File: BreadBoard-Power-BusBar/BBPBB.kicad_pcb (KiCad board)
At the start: 4 copper layers, 53.6 x 5.2 mm, 2 parts, among them J1 Conn_02x02_Odd_Even, J2 Conn_02x02_Odd_Even

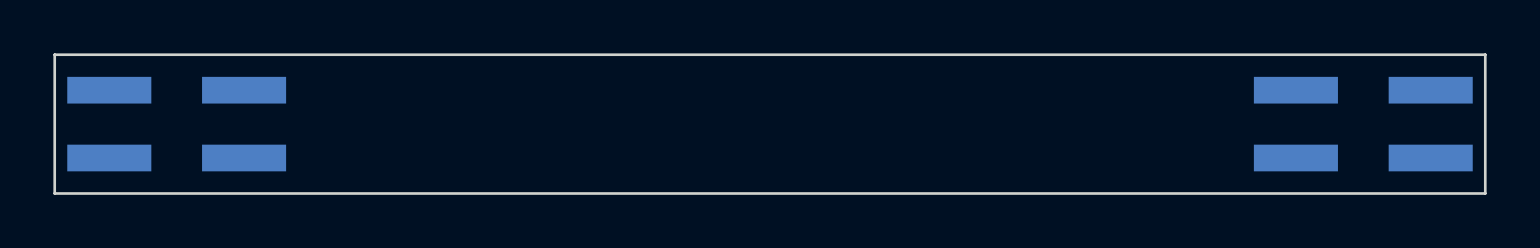
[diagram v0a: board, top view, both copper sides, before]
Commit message: Routed all the power nets through the inner layers.
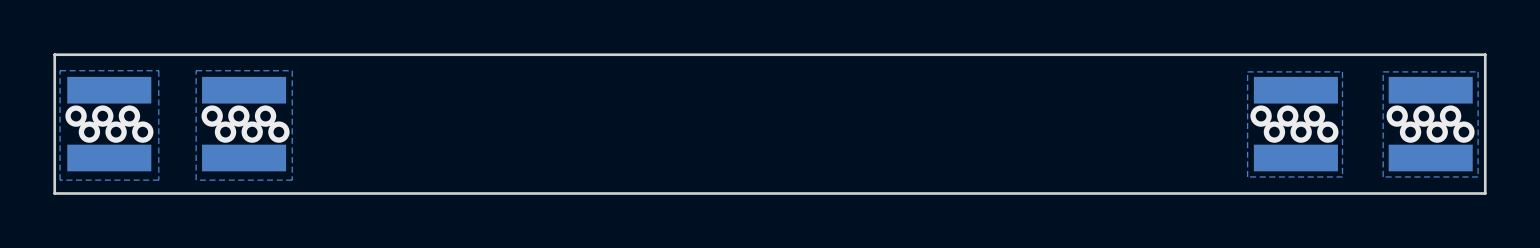
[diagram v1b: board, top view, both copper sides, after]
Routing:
- net /Power-2: vias 0 -> 12
- net /Power-1: vias 0 -> 12
- added copper zone on B.Cu, net /Power-1
- added copper zone on In1.Cu, net /Power-1
- added copper zone on B.Cu, net /Power-2
- added copper zone on In2.Cu, net /Power-2
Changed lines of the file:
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@@
     (thickness 1.6)
     (drawings 9)
-    (tracks 0)
+    (tracks 24)
     (zones 0)
     (modules 2)
@@
   )
   (layers
-    (0 Front signal)
+    (0 F.Cu signal)
     (1 In1.Cu signal)
     (2 In2.Cu signal)
-    (31 Back signal)
+    (31 B.Cu signal)
     (34 B.Paste user)
     (35 F.Paste user)
@@
     (add_net /Power-2)
   )
-  (module Connector_PinHeader_2.54mm:PinHeader_2x02_P2.54mm_Vertical_SMD (layer Back)
+  (module Connector_PinHeader_2.54mm:PinHeader_2x02_P2.54mm_Vertical_SMD (layer B.Cu)
     (at 127.77 100)
     (descr "surface-mounted straight pin header, 2x02, 2.54mm pitch, double rows")
@@
       (effects (font (size 1 1) (thickness 0.15)) (justify mirror))
     )
-    (pad 1 smd rect (at -2.525 1.27) (size 3.15 1) (layers Back B.Paste B.Mask)
+    (pad 1 smd rect (at -2.525 1.27) (size 3.15 1) (layers B.Cu B.Paste B.Mask)
       (net 1 /Power-2))
-    (pad 2 smd rect (at 2.525 1.27) (size 3.15 1) (layers Back B.Paste B.Mask)
+    (pad 2 smd rect (at 2.525 1.27) (size 3.15 1) (layers B.Cu B.Paste B.Mask)
       (net 2 /Power-1))
-    (pad 3 smd rect (at -2.525 -1.27) (size 3.15 1) (layers Back B.Paste B.Mask)
+    (pad 3 smd rect (at -2.525 -1.27) (size 3.15 1) (layers B.Cu B.Paste B.Mask)
       (net 1 /Power-2))
-    (pad 4 smd rect (at 2.525 -1.27) (size 3.15 1) (layers Back B.Paste B.Mask)
+    (pad 4 smd rect (at 2.525 -1.27) (size 3.15 1) (layers B.Cu B.Paste B.Mask)
       (net 2 /Power-1))
     (model ${KISYS3DMOD}/Connector_PinHeader_2.54mm.3dshapes/PinHeader_2x02_P2.54mm_Vertical_SMD.wrl
@@
     )
   )
-  (module Connector_PinHeader_2.54mm:PinHeader_2x02_P2.54mm_Vertical_SMD (layer Back)
+  (module Connector_PinHeader_2.54mm:PinHeader_2x02_P2.54mm_Vertical_SMD (layer B.Cu)
     (at 172.23 100)
     (descr "surface-mounted straight pin header, 2x02, 2.54mm pitch, double rows")
@@
     (fp_line (start -1.59 2.54) (end 2.54 2.54) (layer B.Fab) (width 0.1))
     (fp_line (start 2.54 -2.54) (end -2.54 -2.54) (layer B.Fab) (width 0.1))
-    (pad 4 smd rect (at 2.525 -1.27) (size 3.15 1) (layers Back B.Paste B.Mask)
+    (pad 4 smd rect (at 2.525 -1.27) (size 3.15 1) (layers B.Cu B.Paste B.Mask)
       (net 2 /Power-1))
-    (pad 3 smd rect (at -2.525 -1.27) (size 3.15 1) (layers Back B.Paste B.Mask)
+    (pad 3 smd rect (at -2.525 -1.27) (size 3.15 1) (layers B.Cu B.Paste B.Mask)
       (net 1 /Power-2))
-    (pad 2 smd rect (at 2.525 1.27) (size 3.15 1) (layers Back B.Paste B.Mask)
+    (pad 2 smd rect (at 2.525 1.27) (size 3.15 1) (layers B.Cu B.Paste B.Mask)
       (net 2 /Power-1))
-    (pad 1 smd rect (at -2.525 1.27) (size 3.15 1) (layers Back B.Paste B.Mask)
+    (pad 1 smd rect (at -2.525 1.27) (size 3.15 1) (layers B.Cu B.Paste B.Mask)
       (net 1 /Power-2))
     (model ${KISYS3DMOD}/Connector_PinHeader_2.54mm.3dshapes/PinHeader_2x02_P2.54mm_Vertical_SMD.wrl
@@
   (gr_line (start 176.8 97.4) (end 176.8 102.6) (layer Edge.Cuts) (width 0.1))
   (gr_line (start 123.2 97.4) (end 123.2 102.6) (layer Edge.Cuts) (width 0.1))
+  (via (at 168.9 100.3) (size 0.8) (drill 0.4) (layers F.Cu B.Cu) (net 1))
+  (via (at 170.4 99.7) (size 0.8) (drill 0.4) (layers F.Cu B.Cu) (net 1))
+  (via (at 169.9 100.3) (size 0.8) (drill 0.4) (layers F.Cu B.Cu) (net 1))
+  (via (at 168.4 99.7) (size 0.8) (drill 0.4) (layers F.Cu B.Cu) (net 1))
+  (via (at 170.9 100.3) (size 0.8) (drill 0.4) (layers F.Cu B.Cu) (net 1))
+  (via (at 169.4 99.7) (size 0.8) (drill 0.4) (layers F.Cu B.Cu) (net 1))
+  (via (at 124 99.7) (size 0.8) (drill 0.4) (layers F.Cu B.Cu) (net 1))
+  (via (at 124.5 100.3) (size 0.8) (drill 0.4) (layers F.Cu B.Cu) (net 1))
+  (via (at 125 99.7) (size 0.8) (drill 0.4) (layers F.Cu B.Cu) (net 1))
+  (via (at 125.5 100.3) (size 0.8) (drill 0.4) (layers F.Cu B.Cu) (net 1))
+  (via (at 126 99.7) (size 0.8) (drill 0.4) (layers F.Cu B.Cu) (net 1))
+  (via (at 126.5 100.3) (size 0.8) (drill 0.4) (layers F.Cu B.Cu) (net 1))
+  (via (at 174 100.3) (size 0.8) (drill 0.4) (layers F.Cu B.Cu) (net 2))
+  (via (at 175.5 99.7) (size 0.8) (drill 0.4) (layers F.Cu B.Cu) (net 2))
+  (via (at 175 100.3) (size 0.8) (drill 0.4) (layers F.Cu B.Cu) (net 2))
+  (via (at 173.5 99.7) (size 0.8) (drill 0.4) (layers F.Cu B.Cu) (net 2))
+  (via (at 176 100.3) (size 0.8) (drill 0.4) (layers F.Cu B.Cu) (net 2))
+  (via (at 174.5 99.7) (size 0.8) (drill 0.4) (layers F.Cu B.Cu) (net 2))
+  (via (at 129.6 100.3) (size 0.8) (drill 0.4) (layers F.Cu B.Cu) (net 2))
+  (via (at 131.1 99.7) (size 0.8) (drill 0.4) (layers F.Cu B.Cu) (net 2))
+  (via (at 130.6 100.3) (size 0.8) (drill 0.4) (layers F.Cu B.Cu) (net 2))
+  (via (at 129.1 99.7) (size 0.8) (drill 0.4) (layers F.Cu B.Cu) (net 2))
+  (via (at 131.6 100.3) (size 0.8) (drill 0.4) (layers F.Cu B.Cu) (net 2))
+  (via (at 130.1 99.7) (size 0.8) (drill 0.4) (layers F.Cu B.Cu) (net 2))
+  (zone (net 1) (net_name /Power-2) (layer B.Cu) (hatch edge 0.508)
+    (connect_pads yes (clearance 0.254))
+    (min_thickness 0.254)
+    (fill yes (arc_segments 32) (thermal_gap 0.508) (thermal_bridge_width 0.508))
+    (polygon
+      (pts
+        (xy 127.1 102.1) (xy 123.4 102.1) (xy 123.4 98) (xy 127.1 98)
+      )
+    )
+  )
+  (zone (net 2) (net_name /Power-1) (layer B.Cu) (hatch edge 0.508)
+    (connect_pads yes (clearance 0.254))
+    (min_thickness 0.254)
+    (fill yes (arc_segments 32) (thermal_gap 0.508) (thermal_bridge_width 0.508))
+    (polygon
+      (pts
+        (xy 132.1 102.1) (xy 128.5 102.1) (xy 128.5 98) (xy 132.1 98)
+      )
+    )
+  )
+  (zone (net 2) (net_name /Power-1) (layer In1.Cu) (hatch edge 0.508)
+    (connect_pads yes (clearance 0.508))
+    (min_thickness 0.254)
+    (fill yes (arc_segments 32) (thermal_gap 0.508) (thermal_bridge_width 0.508))
+    (polygon
+      (pts
+        (xy 176.8 102.6) (xy 123.2 102.6) (xy 123.2 97.4) (xy 176.8 97.4)
+      )
+    )
+  )
+  (zone (net 1) (net_name /Power-2) (layer In2.Cu) (hatch edge 0.508)
+    (connect_pads yes (clearance 0.508))
+    (min_thickness 0.254)
+    (fill yes (arc_segments 32) (thermal_gap 0.508) (thermal_bridge_width 0.508))
+    (polygon
+      (pts
+        (xy 176.8 102.6) (xy 123.2 102.6) (xy 123.2 97.4) (xy 176.8 97.4)
+      )
+    )
+  )
+  (zone (net 2) (net_name /Power-1) (layer B.Cu) (hatch edge 0.508)
+    (connect_pads yes (clearance 0.254))
+    (min_thickness 0.254)
+    (fill yes (arc_segments 32) (thermal_gap 0.508) (thermal_bridge_width 0.508))
+    (polygon
+      (pts
+        (xy 176.53 101.981) (xy 172.974 101.981) (xy 172.974 98.044) (xy 176.53 98.044)
+      )
+    )
+  )
+  (zone (net 1) (net_name /Power-2) (layer B.Cu) (hatch edge 0.508)
+    (connect_pads yes (clearance 0.254))
+    (min_thickness 0.254)
+    (fill yes (arc_segments 32) (thermal_gap 0.508) (thermal_bridge_width 0.508))
+    (polygon
+      (pts
+        (xy 171.45 101.981) (xy 167.894 101.981) (xy 167.894 98.044) (xy 171.45 98.044)
+      )
+    )
+  )
 )

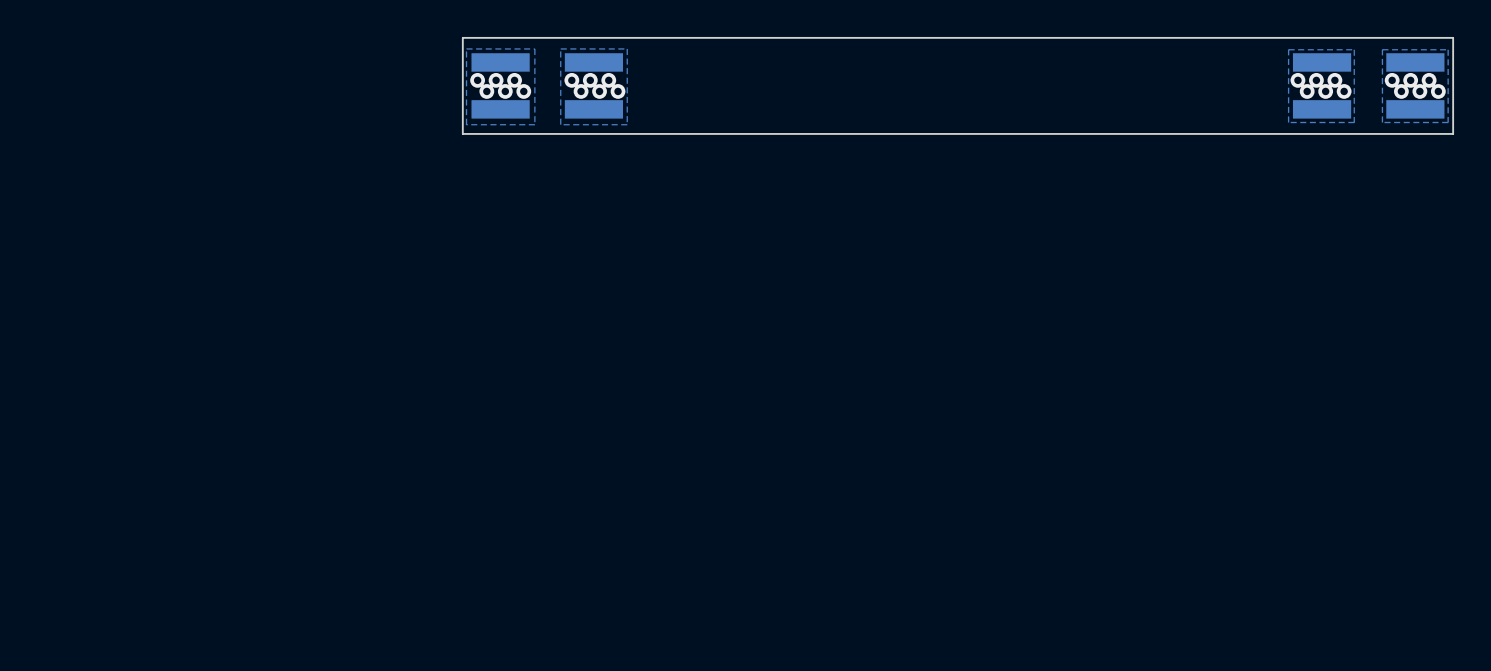
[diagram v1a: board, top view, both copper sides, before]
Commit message: Moved the PCB to have the center at 127|127.
This should make it easier to work with inch / millimeter.
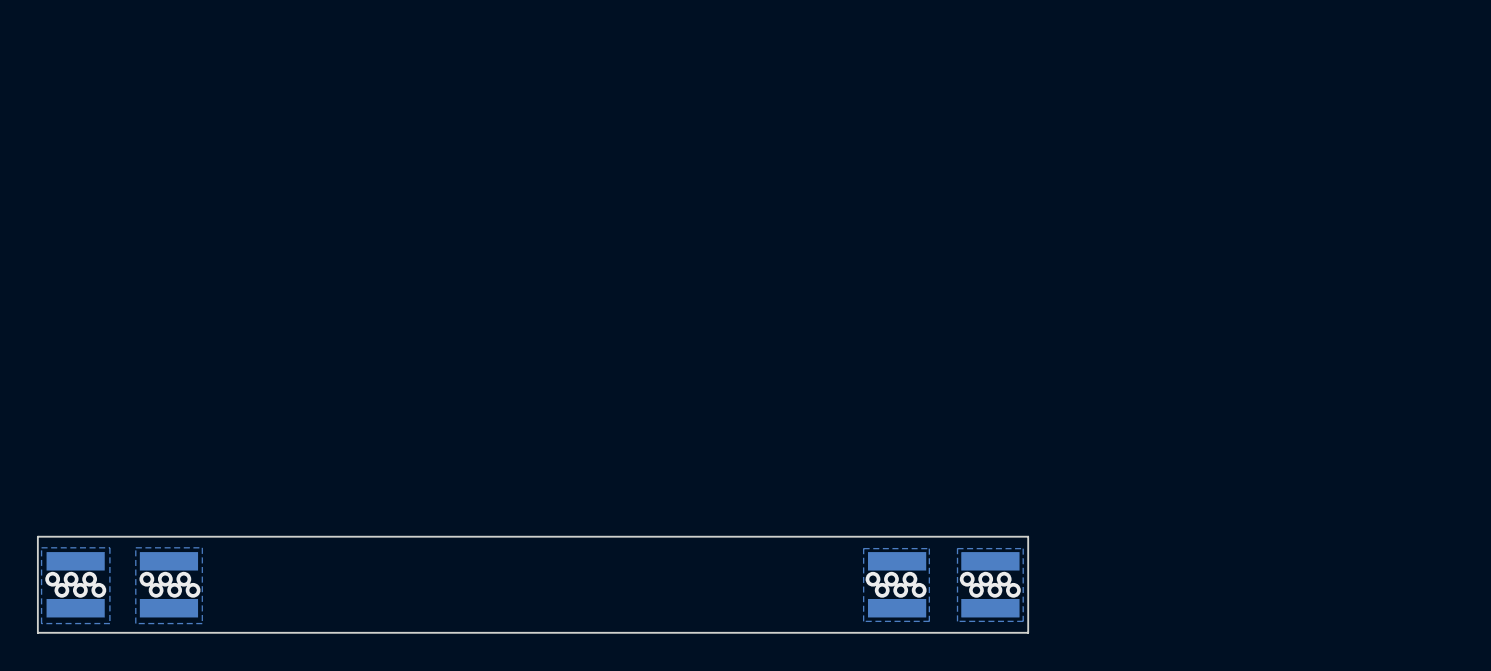
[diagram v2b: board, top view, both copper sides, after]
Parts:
- moved J1 35.5 mm to (104.8, 127.0)
- moved J2 35.5 mm to (149.2, 127.0)
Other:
- board text added: "Origin is at 127 | 127"
- board text removed: "Origin is at 150 | 100"
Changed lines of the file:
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@@
   )
   (module Connector_PinHeader_2.54mm:PinHeader_2x02_P2.54mm_Vertical_SMD (layer B.Cu)
-    (at 127.77 100)
+    (at 104.77 127)
     (descr "surface-mounted straight pin header, 2x02, 2.54mm pitch, double rows")
     (tags "Surface mounted pin header SMD 2x02 2.54mm double row")
@@
   )
   (module Connector_PinHeader_2.54mm:PinHeader_2x02_P2.54mm_Vertical_SMD (layer B.Cu)
-    (at 172.23 100)
+    (at 149.23 127)
     (descr "surface-mounted straight pin header, 2x02, 2.54mm pitch, double rows")
     (tags "Surface mounted pin header SMD 2x02 2.54mm double row")
@@
     )
   )
-  (gr_line (start 126.5 99.5) (end 126.5 100.5) (layer Cmts.User) (width 0.01))
-  (gr_line (start 129.04 99.5) (end 129.04 100.5) (layer Cmts.User) (width 0.01))
-  (gr_line (start 170.96 99.5) (end 170.96 100.5) (layer Cmts.User) (width 0.01))
-  (gr_line (start 173.5 99.5) (end 173.5 100.5) (layer Cmts.User) (width 0.01))
-  (gr_text "Origin is at 150 | 100" (at 275 186.1) (layer Cmts.User)
+  (gr_line (start 103.5 126.5) (end 103.5 127.5) (layer Cmts.User) (width 0.01))
+  (gr_line (start 106.04 126.5) (end 106.04 127.5) (layer Cmts.User) (width 0.01))
+  (gr_line (start 147.96 126.5) (end 147.96 127.5) (layer Cmts.User) (width 0.01))
+  (gr_line (start 150.5 126.5) (end 150.5 127.5) (layer Cmts.User) (width 0.01))
+  (gr_text "Origin is at 127 | 127" (at 275 186.1) (layer Cmts.User)
     (effects (font (size 1.016 1.016) (thickness 0.1524)))
   )
-  (gr_line (start 123.2 97.4) (end 176.8 97.4) (layer Edge.Cuts) (width 0.1))
-  (gr_line (start 176.8 102.6) (end 123.2 102.6) (layer Edge.Cuts) (width 0.1))
-  (gr_line (start 176.8 97.4) (end 176.8 102.6) (layer Edge.Cuts) (width 0.1))
-  (gr_line (start 123.2 97.4) (end 123.2 102.6) (layer Edge.Cuts) (width 0.1))
-  (via (at 168.9 100.3) (size 0.8) (drill 0.4) (layers F.Cu B.Cu) (net 1))
-  (via (at 170.4 99.7) (size 0.8) (drill 0.4) (layers F.Cu B.Cu) (net 1))
-  (via (at 169.9 100.3) (size 0.8) (drill 0.4) (layers F.Cu B.Cu) (net 1))
-  (via (at 168.4 99.7) (size 0.8) (drill 0.4) (layers F.Cu B.Cu) (net 1))
-  (via (at 170.9 100.3) (size 0.8) (drill 0.4) (layers F.Cu B.Cu) (net 1))
-  (via (at 169.4 99.7) (size 0.8) (drill 0.4) (layers F.Cu B.Cu) (net 1))
-  (via (at 124 99.7) (size 0.8) (drill 0.4) (layers F.Cu B.Cu) (net 1))
-  (via (at 124.5 100.3) (size 0.8) (drill 0.4) (layers F.Cu B.Cu) (net 1))
-  (via (at 125 99.7) (size 0.8) (drill 0.4) (layers F.Cu B.Cu) (net 1))
-  (via (at 125.5 100.3) (size 0.8) (drill 0.4) (layers F.Cu B.Cu) (net 1))
-  (via (at 126 99.7) (size 0.8) (drill 0.4) (layers F.Cu B.Cu) (net 1))
-  (via (at 126.5 100.3) (size 0.8) (drill 0.4) (layers F.Cu B.Cu) (net 1))
-  (via (at 174 100.3) (size 0.8) (drill 0.4) (layers F.Cu B.Cu) (net 2))
-  (via (at 175.5 99.7) (size 0.8) (drill 0.4) (layers F.Cu B.Cu) (net 2))
-  (via (at 175 100.3) (size 0.8) (drill 0.4) (layers F.Cu B.Cu) (net 2))
-  (via (at 173.5 99.7) (size 0.8) (drill 0.4) (layers F.Cu B.Cu) (net 2))
-  (via (at 176 100.3) (size 0.8) (drill 0.4) (layers F.Cu B.Cu) (net 2))
-  (via (at 174.5 99.7) (size 0.8) (drill 0.4) (layers F.Cu B.Cu) (net 2))
-  (via (at 129.6 100.3) (size 0.8) (drill 0.4) (layers F.Cu B.Cu) (net 2))
-  (via (at 131.1 99.7) (size 0.8) (drill 0.4) (layers F.Cu B.Cu) (net 2))
-  (via (at 130.6 100.3) (size 0.8) (drill 0.4) (layers F.Cu B.Cu) (net 2))
-  (via (at 129.1 99.7) (size 0.8) (drill 0.4) (layers F.Cu B.Cu) (net 2))
-  (via (at 131.6 100.3) (size 0.8) (drill 0.4) (layers F.Cu B.Cu) (net 2))
-  (via (at 130.1 99.7) (size 0.8) (drill 0.4) (layers F.Cu B.Cu) (net 2))
+  (gr_line (start 100.2 124.4) (end 153.8 124.4) (layer Edge.Cuts) (width 0.1))
+  (gr_line (start 153.8 129.6) (end 100.2 129.6) (layer Edge.Cuts) (width 0.1))
+  (gr_line (start 153.8 124.4) (end 153.8 129.6) (layer Edge.Cuts) (width 0.1))
+  (gr_line (start 100.2 124.4) (end 100.2 129.6) (layer Edge.Cuts) (width 0.1))
+  (via (at 145.9 127.3) (size 0.8) (drill 0.4) (layers F.Cu B.Cu) (net 1))
+  (via (at 147.4 126.7) (size 0.8) (drill 0.4) (layers F.Cu B.Cu) (net 1))
+  (via (at 146.9 127.3) (size 0.8) (drill 0.4) (layers F.Cu B.Cu) (net 1))
+  (via (at 145.4 126.7) (size 0.8) (drill 0.4) (layers F.Cu B.Cu) (net 1))
+  (via (at 147.9 127.3) (size 0.8) (drill 0.4) (layers F.Cu B.Cu) (net 1))
+  (via (at 146.4 126.7) (size 0.8) (drill 0.4) (layers F.Cu B.Cu) (net 1))
+  (via (at 101 126.7) (size 0.8) (drill 0.4) (layers F.Cu B.Cu) (net 1))
+  (via (at 101.5 127.3) (size 0.8) (drill 0.4) (layers F.Cu B.Cu) (net 1))
+  (via (at 102 126.7) (size 0.8) (drill 0.4) (layers F.Cu B.Cu) (net 1))
+  (via (at 102.5 127.3) (size 0.8) (drill 0.4) (layers F.Cu B.Cu) (net 1))
+  (via (at 103 126.7) (size 0.8) (drill 0.4) (layers F.Cu B.Cu) (net 1))
+  (via (at 103.5 127.3) (size 0.8) (drill 0.4) (layers F.Cu B.Cu) (net 1))
+  (via (at 151 127.3) (size 0.8) (drill 0.4) (layers F.Cu B.Cu) (net 2))
+  (via (at 152.5 126.7) (size 0.8) (drill 0.4) (layers F.Cu B.Cu) (net 2))
+  (via (at 152 127.3) (size 0.8) (drill 0.4) (layers F.Cu B.Cu) (net 2))
+  (via (at 150.5 126.7) (size 0.8) (drill 0.4) (layers F.Cu B.Cu) (net 2))
+  (via (at 153 127.3) (size 0.8) (drill 0.4) (layers F.Cu B.Cu) (net 2))
+  (via (at 151.5 126.7) (size 0.8) (drill 0.4) (layers F.Cu B.Cu) (net 2))
+  (via (at 106.6 127.3) (size 0.8) (drill 0.4) (layers F.Cu B.Cu) (net 2))
+  (via (at 108.1 126.7) (size 0.8) (drill 0.4) (layers F.Cu B.Cu) (net 2))
+  (via (at 107.6 127.3) (size 0.8) (drill 0.4) (layers F.Cu B.Cu) (net 2))
+  (via (at 106.1 126.7) (size 0.8) (drill 0.4) (layers F.Cu B.Cu) (net 2))
+  (via (at 108.6 127.3) (size 0.8) (drill 0.4) (layers F.Cu B.Cu) (net 2))
+  (via (at 107.1 126.7) (size 0.8) (drill 0.4) (layers F.Cu B.Cu) (net 2))
   (zone (net 1) (net_name /Power-2) (layer B.Cu) (hatch edge 0.508)
     (connect_pads yes (clearance 0.254))
@@
     (polygon
       (pts
-        (xy 127.1 102.1) (xy 123.4 102.1) (xy 123.4 98) (xy 127.1 98)
+        (xy 104.1 129.1) (xy 100.4 129.1) (xy 100.4 125) (xy 104.1 125)
       )
     )
@@
     (polygon
       (pts
-        (xy 132.1 102.1) (xy 128.5 102.1) (xy 128.5 98) (xy 132.1 98)
+        (xy 109.1 129.1) (xy 105.5 129.1) (xy 105.5 125) (xy 109.1 125)
       )
     )
@@
     (polygon
       (pts
-        (xy 176.8 102.6) (xy 123.2 102.6) (xy 123.2 97.4) (xy 176.8 97.4)
+        (xy 153.8 129.6) (xy 100.2 129.6) (xy 100.2 124.4) (xy 153.8 124.4)
       )
     )
@@
     (polygon
       (pts
-        (xy 176.8 102.6) (xy 123.2 102.6) (xy 123.2 97.4) (xy 176.8 97.4)
+        (xy 153.8 129.6) (xy 100.2 129.6) (xy 100.2 124.4) (xy 153.8 124.4)
       )
     )
@@
     (polygon
       (pts
-        (xy 176.53 101.981) (xy 172.974 101.981) (xy 172.974 98.044) (xy 176.53 98.044)
+        (xy 153.53 128.981) (xy 149.974 128.981) (xy 149.974 125.044) (xy 153.53 125.044)
       )
     )
@@
     (polygon
       (pts
-        (xy 171.45 101.981) (xy 167.894 101.981) (xy 167.894 98.044) (xy 171.45 98.044)
-      )
-    )
+        (xy 148.45 128.981) (xy 144.894 128.981) (xy 144.894 125.044) (xy 148.45 125.044)
+      )
+    )
